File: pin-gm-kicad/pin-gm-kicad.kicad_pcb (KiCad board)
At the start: 2 copper layers, 36 parts, among them U1 TL072, U2 LM358

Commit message: kb semmi
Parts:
- L1: value L -> 1m; footprint Inductor_SMD:L_Bourns_SRR0604_homemade -> Homemade:L_Bourns_SRR0604_homemade
- moved D2 69.8 mm to (144.1, 49.0), turned to 90 degrees
- moved LS1 65.4 mm to (248.7, 53.0)
- moved D1 63.8 mm to (144.2, 58.6), turned to 90 degrees
- moved BT1 57.9 mm to (230.5, 67.7)
- moved D3 49.3 mm to (143.7, 40.9), turned to 90 degrees
- moved U2 46.8 mm to (154.6, 33.6)
- moved D4 46.7 mm to (143.8, 32.7), turned to 90 degrees
- moved L1 29.3 mm to (167.0, 22.2)
- moved U1 23.8 mm to (187.8, 27.5)
- renumbered C13 to C10, C14 to C11, C8 to C12, C9 to C13, C10 to C14, C11 to C2, C2 to C3, C3 to C6, C12 to C7, C6 to C8, C7 to C9, D4 to D1, D3 to D2, D2 to D3, D1 to D4, R9 to R1, R5 to R10, R6 to R11, R7 to R12, R8 to R13, R10 to R2, R11 to R3, R12 to R4, R3 to R5, R2 to R6, R13 to R7, R4 to R8, R14 to R9, U2 to U1, U1 to U2

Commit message: kész vannak a footprintek
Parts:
- added C15: 47u, Capacitor_SMD:C_1210_3225Metric_Pad1.33x2.70mm_HandSolder, F.Cu at (318.9, 33.7)
- added C4: 10-40p, Homemade:C_trimmer_D10mm_homemade, F.Cu at (266.1, 26.8)
- C11, C14: value 47u -> 100n; footprint Capacitor_SMD:C_1210_3225Metric_Pad1.33x2.70mm_HandSolder -> Capacitor_SMD:C_1206_3216Metric_Pad1.33x1.80mm_HandSolder
- C12: value 10p -> 47u; footprint Capacitor_SMD:C_1206_3216Metric_Pad1.33x1.80mm_HandSolder -> Capacitor_SMD:C_1210_3225Metric_Pad1.33x2.70mm_HandSolder
- C13, C7, C8: value 100n -> 10p
- C6: value 10p -> 100n
- R9: footprint Resistor_SMD:R_1206_3216Metric -> Resistor_SMD:R_1206_3216Metric_Pad1.30x1.75mm_HandSolder
- moved D1 183.6 mm to (323.0, 16.8), turned to 0 degrees
- moved D3 174.2 mm to (317.5, 28.6), turned to 0 degrees
- moved D2 159.7 mm to (303.2, 36.0), turned to 0 degrees
- moved D4 151.3 mm to (294.8, 42.4), turned to 0 degrees
- moved C10 145.7 mm to (361.5, 38.6)
- moved C12 135.9 mm to (332.7, 16.0)
- moved C8 134.3 mm to (336.0, 48.4), turned to 90 degrees
- moved R9 132.1 mm to (324.9, 33.2)
- moved R1 131.7 mm to (339.1, 23.1)
- moved R6 131.7 mm to (339.1, 26.4)
- moved C3 125.6 mm to (341.5, 64.8), turned to 90 degrees
- moved C13 124.5 mm to (348.8, 48.2)
- moved R8 122.9 mm to (342.4, 18.9)
- moved R11 121.8 mm to (333.2, 28.0)
- moved C2 121.8 mm to (327.2, 24.7)
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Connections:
- net Net-(C3-Pad1) renamed /Diode_Cathode
- C10 pad 1: VCC -> Net-(C10-Pad1)
- C12 pad 1: Net-(C12-Pad1) -> VCC
- C12 pad 2: Net-(C12-Pad2) -> GND
- C13 pad 2: GND -> Net-(C13-Pad2)
- C14 pad 1: Net-(C13-Pad1) -> Net-(C14-Pad1)
- C6 pad 1: Net-(C3-Pad2) -> Net-(C6-Pad1)
- C7 pad 1: Net-(C7-Pad1) -> Net-(C3-Pad2)
- C7 pad 2: Net-(C7-Pad2) -> GND
- C8 pad 1: Net-(C6-Pad2) -> Net-(C3-Pad2)
- C9 pad 1: Net-(C9-Pad1) -> Net-(C8-Pad2)
- C9 pad 2: GND -> Net-(C9-Pad2)
- L1 pad 1: Net-(C13-Pad1) -> Net-(C14-Pad1)
- LS1 pad 1: Net-(C7-Pad2) -> Net-(C6-Pad2)
- R1 pad 1: Net-(C12-Pad2) -> Net-(C13-Pad2)
- R10 pad 1: Net-(C8-Pad2) -> Net-(C9-Pad2)
- R10 pad 2: Net-(C12-Pad1) -> Net-(C13-Pad1)
- R11 pad 1: Net-(C13-Pad1) -> Net-(C14-Pad1)
- R11 pad 2: Net-(C9-Pad1) -> Net-(C10-Pad1)
- R12 pad 1: Net-(C9-Pad1) -> Net-(C10-Pad1)
- R13 pad 1: Net-(C12-Pad1) -> Net-(C13-Pad1)
- R13 pad 2: Net-(C12-Pad2) -> Net-(C13-Pad2)
- R5 pad 1: Net-(C13-Pad1) -> Net-(C14-Pad1)
- R8 pad 2: Net-(C6-Pad2) -> Net-(R8-Pad2)
- R9 pad 2: Net-(C7-Pad1) -> Net-(C6-Pad1)
- U2 pad 1: Net-(C6-Pad2) -> Net-(R8-Pad2)
- U2 pad 5: Net-(C9-Pad1) -> Net-(C10-Pad1)
- U2 pad 6: Net-(C12-Pad1) -> Net-(C13-Pad1)
- U2 pad 7: Net-(C12-Pad2) -> Net-(C13-Pad2)
- U2 pad 8: Net-(C13-Pad1) -> Net-(C14-Pad1)
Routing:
- net Net-(C3-Pad2): track 0.00 -> 0.81 mm

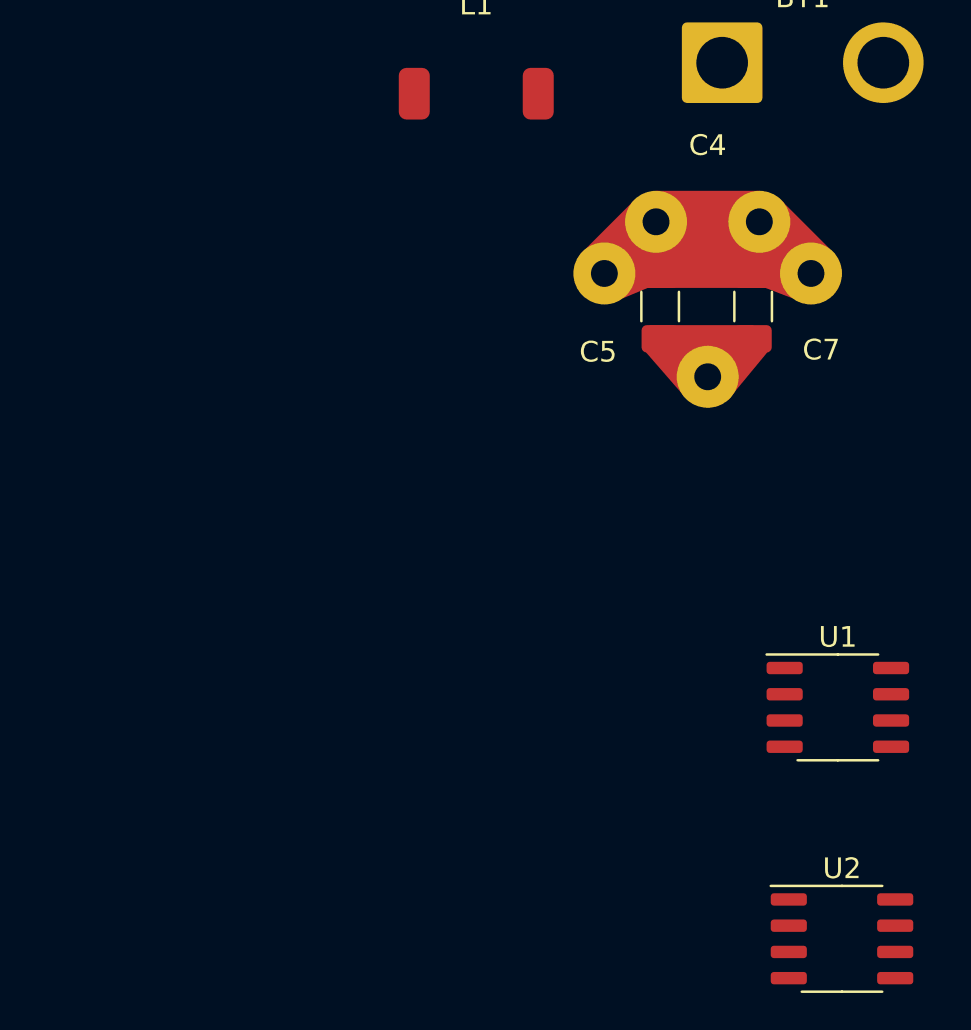
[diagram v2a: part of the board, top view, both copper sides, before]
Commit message: egyéni footprintek
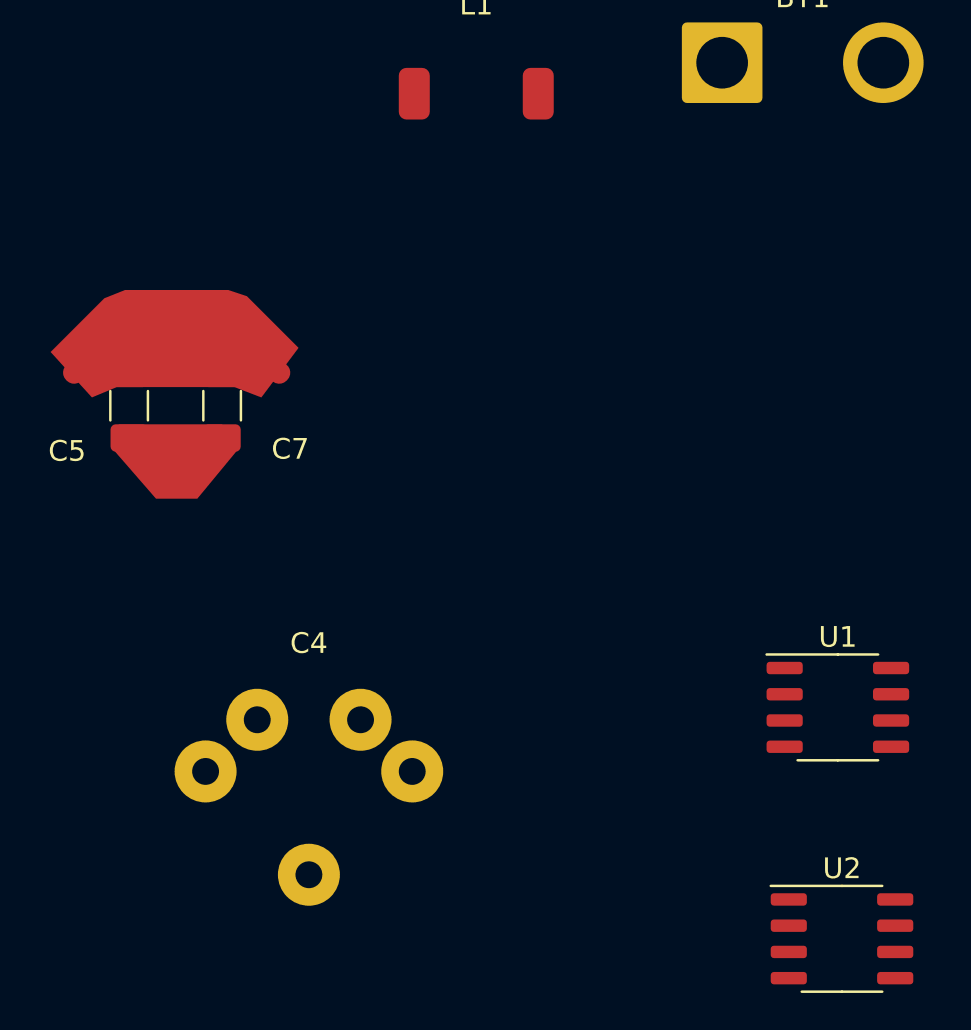
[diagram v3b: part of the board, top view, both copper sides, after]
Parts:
- moved C4 30.9 mm to (246.8, 50.9)
- moved C5 26.1 mm to (238.1, 33.2)
- moved C7 26.1 mm to (242.6, 33.2)
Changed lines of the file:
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@@
   (net 22 "/Diode_Cathode")
   (footprint "Capacitor_SMD:C_1206_3216Metric_Pad1.33x1.80mm_HandSolder" (layer "F.Cu")
-    (at 263.77 28.38 -90)
+    (at 238.07 33.18 -90)
     (descr "Capacitor SMD 1206 (3216 Metric), square (rectangular) end terminal, IPC_7351 nominal with elongated pad for handsoldering. (Body size source: IPC-SM-782 page 76, https://www.pcb-3d.com/wordpress/wp-content/uploads/ipc-sm-782a_amendment_1_and_2.pdf), generated with kicad-footprint-generator")
     (tags "capacitor handsolder")
@@
   )
   (footprint "Homemade:C_trimmer_D10mm_homemade" (layer "F.Cu")
-    (at 266.07 26.78)
+    (at 246.77 50.88)
     (property "Sheetfile" "pin-gm-kicad.kicad_sch")
     (property "Sheetname" "")
@@
   )
   (footprint "Capacitor_SMD:C_1206_3216Metric_Pad1.33x1.80mm_HandSolder" (layer "F.Cu")
-    (at 268.27 28.38 -90)
+    (at 242.57 33.18 -90)
     (descr "Capacitor SMD 1206 (3216 Metric), square (rectangular) end terminal, IPC_7351 nominal with elongated pad for handsoldering. (Body size source: IPC-SM-782 page 76, https://www.pcb-3d.com/wordpress/wp-content/uploads/ipc-sm-782a_amendment_1_and_2.pdf), generated with kicad-footprint-generator")
     (tags "capacitor handsolder")
@@
   (gr_poly
     (pts
-      (xy 269.47 23.08)
-      (xy 271.97 25.58)
-      (xy 270.17 27.98)
-      (xy 268.87 27.48)
-      (xy 263.17 27.48)
-      (xy 261.97 27.98)
-      (xy 259.97 25.78)
-      (xy 262.57 23.18)
-      (xy 263.57 22.78)
-      (xy 268.57 22.78)
+      (xy 243.77 27.88)
+      (xy 246.27 30.38)
+      (xy 244.47 32.78)
+      (xy 243.17 32.28)
+      (xy 237.47 32.28)
+      (xy 236.27 32.78)
+      (xy 234.27 30.58)
+      (xy 236.87 27.98)
+      (xy 237.87 27.58)
+      (xy 242.87 27.58)
     ) (layer "F.Cu") (width 0) (fill solid))
   (gr_poly
     (pts
-      (xy 268.97 30.58)
-      (xy 267.07 32.88)
-      (xy 265.07 32.88)
-      (xy 263.07 30.58)
-      (xy 263.27 29.28)
-      (xy 268.27 29.28)
+      (xy 243.27 35.38)
+      (xy 241.37 37.68)
+      (xy 239.37 37.68)
+      (xy 237.37 35.38)
+      (xy 237.57 34.08)
+      (xy 242.57 34.08)
     ) (layer "F.Cu") (width 0) (fill solid))
-  (segment (start 268.27 29.9425) (end 267.9075 29.9425) (width 1) (layer "F.Cu") (net 2))
-  (segment (start 263.77 24.48) (end 263.57 24.28) (width 1) (layer "F.Cu") (net 6))
-  (segment (start 271.0325 26.8175) (end 271.07 26.78) (width 1) (layer "F.Cu") (net 6))
-  (segment (start 261.1075 26.8175) (end 261.07 26.78) (width 1) (layer "F.Cu") (net 6))
-  (segment (start 268.27 24.58) (end 268.57 24.28) (width 1) (layer "F.Cu") (net 6))
-  (group "" (id aad7204c-87a9-4352-99ae-9b3ae95e291d)
-    (members
-      05fa7b1a-8ed3-4b32-82c0-6b7ad7df3417
-      53b9b647-a93e-4072-ae64-0d7e34db731d
-      7ca82459-edb4-4dd3-9a35-77ce0d560cd7
-      85b94d87-d148-42c7-8567-8d445153713a
-      8d4e2929-4411-4597-8c87-8dcb1df47ea0
-      9e087255-9025-4d18-8f1e-a51ba1c100e6
-      abd838be-7290-417a-825f-9081d72b9963
-      f4518254-120c-4e1c-ac33-d2b23fdc0fc7
-      f8d28331-eeae-4d87-867f-0a521759c2f1
-      fd23d600-64d7-41d7-a114-849a5c445d5c
-    )
-  )
+  (segment (start 242.57 34.7425) (end 242.2075 34.7425) (width 1) (layer "F.Cu") (net 2))
+  (segment (start 238.07 29.28) (end 237.87 29.08) (width 1) (layer "F.Cu") (net 6))
+  (segment (start 245.3325 31.6175) (end 245.37 31.58) (width 1) (layer "F.Cu") (net 6))
+  (segment (start 235.4075 31.6175) (end 235.37 31.58) (width 1) (layer "F.Cu") (net 6))
+  (segment (start 242.57 29.38) (end 242.87 29.08) (width 1) (layer "F.Cu") (net 6))
 )

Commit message: kezdetleges layout
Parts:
- BT1, LS1: footprint Connector_Wire:SolderWire-2sqmm_1x02_P7.8mm_D2mm_OD3.9mm -> Homemade:SolderWire-homemade
- C1, C10, C11, C13, C14, C2, C3, C5, C6, C7, C8, C9: footprint Capacitor_SMD:C_1206_3216Metric_Pad1.33x1.80mm_HandSolder -> Homemade:C_1206_3216Metric_homemade
- C12, C15: footprint Capacitor_SMD:C_1210_3225Metric_Pad1.33x2.70mm_HandSolder -> Homemade:C_1210_3225Metric_homemade
- D1, D2, D3, D4: footprint OptoDevice:Osram_DIL2_4.3x4.65mm_P5.08mm -> Homemade:BPW34_homemade
- R1, R10, R11, R12, R13, R2, R3, R4, R5, R6, R7, R8, R9: footprint Resistor_SMD:R_1206_3216Metric_Pad1.30x1.75mm_HandSolder -> Homemade:R_1206_3216Metric_homemade
- RV1: footprint Potentiometer_THT:Potentiometer_Piher_PT-10-V10_Vertical -> Homemade:Potentiometer_D10_vert_homemade
- U1, U2: footprint Package_SO:SO-8_3.9x4.9mm_P1.27mm -> Homemade:SO-8_3.9x4.9mm_homemade
- moved D1 265.2 mm to (60.5, 54.2)
- moved D3 260.3 mm to (58.0, 49.2), turned to 180 degrees
- moved D2 245.9 mm to (58.0, 54.2), turned to 180 degrees
- moved D4 234.4 mm to (60.5, 49.2)
- moved U2 213.4 mm to (59.2, 62.7), turned to -90 degrees
- moved LS1 95.2 mm to (210.5, 63.7)
- moved L1 10.6 mm to (259.2, 27.7)
- moved C7 6.79 mm to (247.2, 28.2)
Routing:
- net Net-(C3-Pad2): track 0.81 -> 0.00 mm

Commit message: kis haladás
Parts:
- moved C4 219.3 mm to (28.0, 65.0)
- moved C7 216.1 mm to (36.5, 76.0), turned to 0 degrees
- moved L1 211.8 mm to (54.0, 80.0)
- moved C5 205.5 mm to (36.5, 73.0), turned to 0 degrees
- moved R11 129.1 mm to (205.2, 45.1)
- moved R2 129.1 mm to (190.9, 54.6)
- moved R3 129.1 mm to (188.5, 61.1)
- moved R5 129.1 mm to (205.2, 41.9)
- moved R8 129.1 mm to (214.4, 36.0)
- moved C1 129.1 mm to (176.5, 61.1)
- moved C11 129.1 mm to (208.4, 36.9)
- moved C12 129.1 mm to (204.7, 33.1)
- moved C14 129.1 mm to (199.2, 45.2)
- moved C15 129.1 mm to (191.0, 50.8)
- moved C2 129.1 mm to (199.2, 41.9)
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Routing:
- net GND: track 0.54 -> 0.00 mm
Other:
- board outline added: 70 x 84 mm

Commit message: kb elhelyezve
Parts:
- added H1: MountingHole_Pad, Homemade:Mounting_Hole_Dhole4mm_homemade, F.Cu at (70.0, 72.5)
- added H2: MountingHole_Pad, Homemade:Mounting_Hole_Dhole4mm_homemade, F.Cu at (100.0, 72.5)
- moved C10 154.5 mm to (82.8, 89.8), turned to 180 degrees
- moved R8 145.4 mm to (76.5, 82.2), turned to 90 degrees
- moved R6 144.4 mm to (73.8, 88.0), turned to -90 degrees
- moved C3 141.5 mm to (72.0, 83.8), turned to 180 degrees
- moved R4 139.4 mm to (58.0, 64.2)
- moved C8 136.9 mm to (72.0, 80.8), turned to 0 degrees
- moved R13 136.5 mm to (91.8, 87.5), turned to 90 degrees
- moved R5 135.6 mm to (79.5, 92.8), turned to 180 degrees
- moved C13 134.2 mm to (88.5, 87.5), turned to 90 degrees
- moved C2 130.3 mm to (69.8, 56.5), turned to 90 degrees
- moved R11 129.3 mm to (85.0, 92.8)
- moved R7 125.9 mm to (77.8, 62.0)
- moved R12 125.1 mm to (82.8, 86.8), turned to 180 degrees
- moved R1 124.1 mm to (95.2, 84.5), turned to 90 degrees
- moved R2 118.0 mm to (73.0, 52.0), turned to 180 degrees
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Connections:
- R8 pad 2: Net-(R8-Pad2) -> Net-(C8-Pad2)
- U2 pad 1: Net-(R8-Pad2) -> Net-(C8-Pad2)
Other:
- board size 70 x 84 mm -> 62 x 45 mm

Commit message: kb kész a layout
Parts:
- moved C12 22.2 mm to (106.2, 70.0), turned to 0 degrees
- moved C11 16.2 mm to (106.2, 65.8), turned to 0 degrees
- moved R4 4.50 mm to (62.5, 64.2)
- moved R3 3.75 mm to (75.8, 62.0)
- moved R7 3.75 mm to (81.5, 62.0)
- moved U1 3.25 mm to (79.0, 56.8)
- moved R11 2.00 mm to (87.0, 92.8)
- moved C2 1.75 mm to (71.5, 56.5)
- moved L1 0.35 mm to (111.8, 84.8)
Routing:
- net VCC: track 0.00 -> 57.6 mm, vias 0 -> 2
- net Net-(C14-Pad1): track 0.00 -> 51.7 mm, vias 0 -> 3
- net Net-(C2-Pad1): track 0.00 -> 45.9 mm, vias 0 -> 2
- net /Diode_Cathode: track 0.00 -> 28.4 mm
- net Net-(R9-Pad1): track 0.00 -> 23.8 mm
- net Net-(C8-Pad2): track 0.00 -> 21.8 mm, vias 0 -> 2
- net Net-(C1-Pad1): track 0.00 -> 15.7 mm
- net Net-(C13-Pad2): track 0.00 -> 15.6 mm, vias 0 -> 2
- net Net-(R4-Pad2): track 0.00 -> 15.2 mm, vias 0 -> 2
- net Net-(C2-Pad2): track 0.00 -> 14.9 mm
- net Net-(C13-Pad1): track 0.00 -> 14.8 mm, vias 0 -> 2
- net Net-(C3-Pad2): track 0.00 -> 14.5 mm
- net Net-(C10-Pad1): track 0.00 -> 11.5 mm
- net Net-(R4-Pad1): track 0.00 -> 9.41 mm
- net Net-(C6-Pad1): track 0.00 -> 9.24 mm
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- added copper zone on B.Cu, net GND
- added copper zone on F.Cu, net GND
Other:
- outline, holes or cut-outs redrawn

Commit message: mostmár tuti jó a layout
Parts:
- moved R9 5.00 mm to (101.0, 57.5)
- moved C12 4.50 mm to (106.2, 65.5)
- moved C15 4.07 mm to (102.5, 84.5)
- moved C4 4.03 mm to (61.5, 83.8)
- moved C11 4.00 mm to (106.2, 61.8)
- moved R5 4.00 mm to (83.5, 92.8)
- moved C1 3.50 mm to (76.5, 91.5), turned to 90 degrees
- moved R11 3.50 mm to (90.5, 92.8)
- moved R6 3.50 mm to (73.8, 91.5), turned to 90 degrees
- moved C14 3.01 mm to (98.8, 84.5)
- moved C7 3.00 mm to (68.2, 90.0)
- moved C5 2.75 mm to (68.2, 92.8)
- moved C3 2.25 mm to (72.0, 86.0)
- moved C8 2.25 mm to (72.0, 83.0)
- moved BT1 0.50 mm to (112.0, 76.8)
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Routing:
- net Net-(C14-Pad1): track 51.7 -> 46.4 mm
- net Net-(C6-Pad1): track 9.24 -> 4.00 mm
- net Net-(R9-Pad1): track 23.8 -> 19.2 mm
- net Net-(C1-Pad1): track 15.7 -> 19.8 mm
- net Net-(C10-Pad1): track 11.5 -> 14.9 mm
- net Net-(C13-Pad1): track 14.8 -> 16.2 mm
- net /Diode_Cathode: track 28.4 -> 29.8 mm
- net Net-(C8-Pad2): track 21.8 -> 23.0 mm
- net VCC: track 57.6 -> 56.8 mm
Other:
- board text added: "+"
- board text added: "-"
- board text added: "Audio"
- board text added: "Geigerle"
